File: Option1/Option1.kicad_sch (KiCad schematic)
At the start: 0 parts

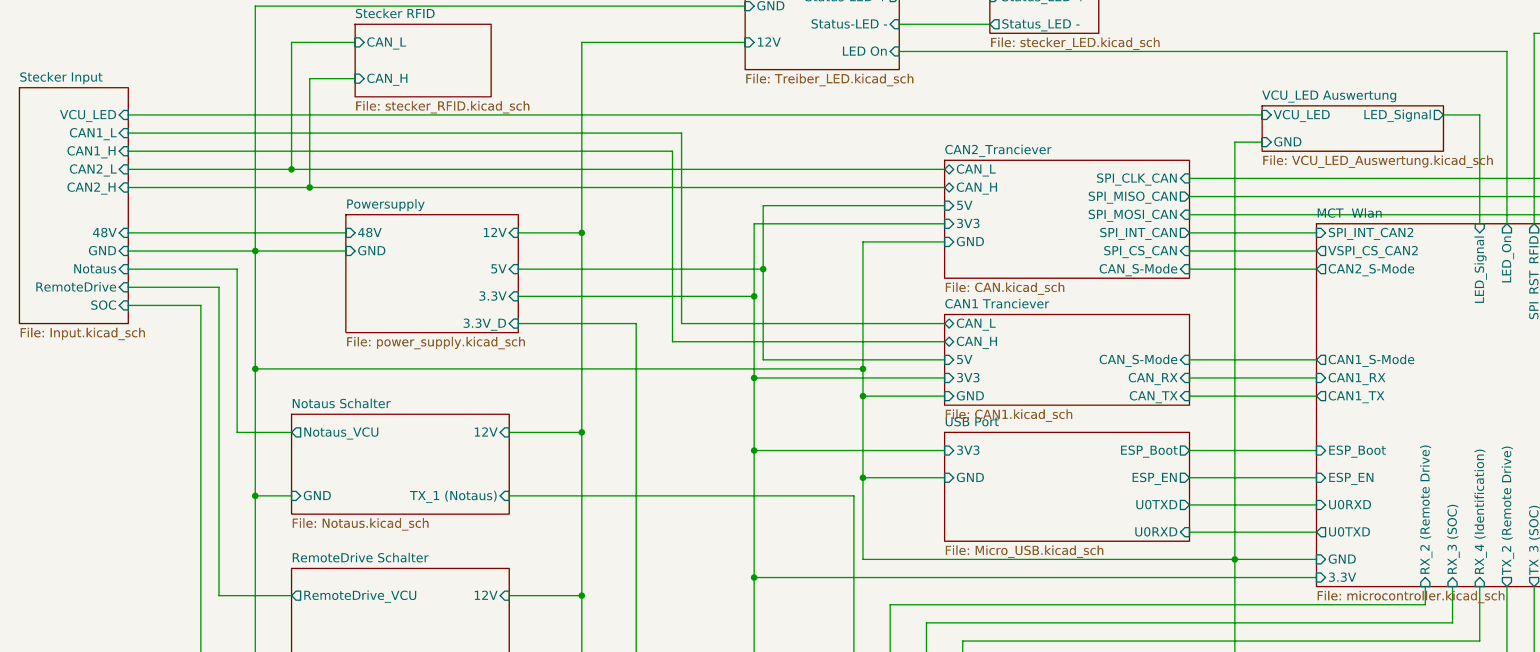
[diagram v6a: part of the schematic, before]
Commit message: USB Schaltung angepasst, Transistoren korrigiert, Stecker ausgetauscht, Dioden hinzugefügt
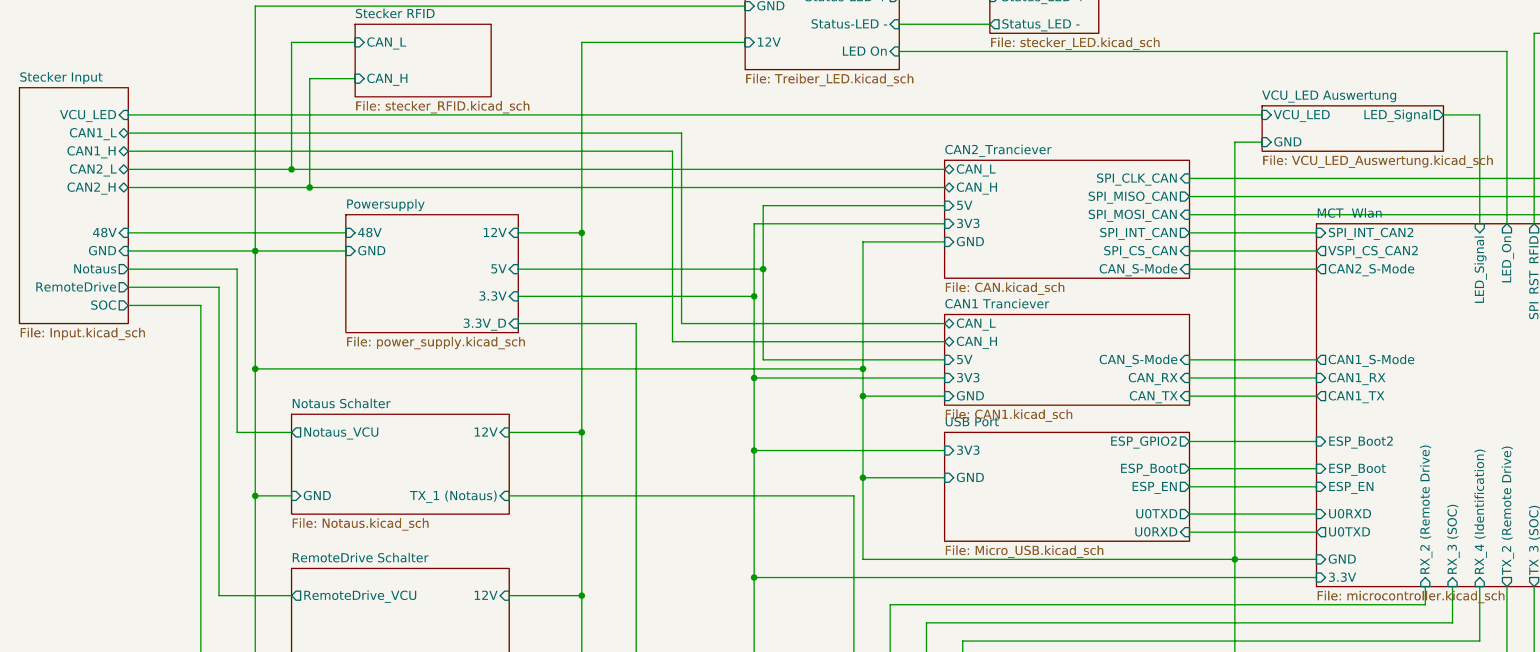
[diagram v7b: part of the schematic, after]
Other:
- sheet MCT  Wlan ports: added ESP_Boot2; removed none
- sheet USB Port ports: added ESP_GPIO2; removed none
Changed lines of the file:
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@@
 	(wire
 		(pts
-			(xy 187.96 83.82) (xy 205.74 83.82)
+			(xy 187.96 86.36) (xy 205.74 86.36)
 		)
 		(stroke
@@
 	(wire
 		(pts
+			(xy 187.96 88.9) (xy 205.74 88.9)
+		)
+		(stroke
+			(width 0)
+			(type default)
+		)
+	)
+	(wire
+		(pts
 			(xy 57.15 72.39) (xy 142.24 72.39)
 		)
@@
 	(wire
 		(pts
-			(xy 187.96 91.44) (xy 205.74 91.44)
-		)
-		(stroke
-			(width 0)
-			(type default)
-		)
-	)
-	(wire
-		(pts
 			(xy 39.37 36.83) (xy 198.12 36.83)
 		)
@@
 	(wire
 		(pts
-			(xy 205.74 87.63) (xy 187.96 87.63)
-		)
-		(stroke
-			(width 0)
-			(type default)
-		)
-	)
-	(wire
-		(pts
 			(xy 261.62 73.66) (xy 264.16 73.66)
 		)
@@
 	(wire
 		(pts
+			(xy 187.96 82.55) (xy 205.74 82.55)
+		)
+		(stroke
+			(width 0)
+			(type default)
+		)
+	)
+	(wire
+		(pts
 			(xy 92.71 113.03) (xy 232.41 113.03)
 		)
@@
 			(type default)
 			(color 0 133 255 1)
+		)
+	)
+	(wire
+		(pts
+			(xy 187.96 92.71) (xy 205.74 92.71)
+		)
+		(stroke
+			(width 0)
+			(type default)
 		)
 	)
@@
 		)
 		(pin "U0TXD" output
-			(at 187.96 91.44 0)
+			(at 187.96 92.71 0)
 			(effects
 				(font
@@
 		)
 		(pin "ESP_EN" output
-			(at 187.96 87.63 0)
+			(at 187.96 88.9 0)
 			(effects
 				(font
@@
 		)
 		(pin "ESP_Boot" output
-			(at 187.96 83.82 0)
+			(at 187.96 86.36 0)
 			(effects
 				(font
@@
 				)
 				(justify left)
+			)
+		)
+		(pin "ESP_GPIO2" output
+			(at 187.96 82.55 0)
+			(effects
+				(font
+					(size 1.27 1.27)
+				)
+				(justify right)
 			)
 		)
@@
 		)
 		(pin "ESP_EN" input
-			(at 205.74 87.63 180)
+			(at 205.74 88.9 180)
 			(effects
 				(font
@@
 		)
 		(pin "ESP_Boot" input
-			(at 205.74 83.82 180)
+			(at 205.74 86.36 180)
 			(effects
 				(font
@@
 		)
 		(pin "U0RXD" input
-			(at 205.74 91.44 180)
+			(at 205.74 92.71 180)
 			(effects
 				(font
@@
 		(pin "SPI_INT_CAN2" input
 			(at 205.74 53.34 180)
+			(effects
+				(font
+					(size 1.27 1.27)
+				)
+				(justify left)
+			)
+		)
+		(pin "ESP_Boot2" input
+			(at 205.74 82.55 180)
 			(effects
 				(font
@@
 			)
 		)
-		(pin "CAN2_L" input
-			(at 39.37 44.45 0)
-			(effects
-				(font
-					(size 1.27 1.27)
-				)
-				(justify right)
-			)
-		)
 		(pin "48V" input
 			(at 39.37 53.34 0)
@@
 			)
 		)
-		(pin "CAN2_H" input
-			(at 39.37 46.99 0)
-			(effects
-				(font
-					(size 1.27 1.27)
-				)
-				(justify right)
-			)
-		)
-		(pin "Notaus" input
-			(at 39.37 58.42 0)
-			(effects
-				(font
-					(size 1.27 1.27)
-				)
-				(justify right)
-			)
-		)
 		(pin "GND" input
 			(at 39.37 55.88 0)
@@
 			)
 		)
-		(pin "SOC" input
-			(at 39.37 63.5 0)
-			(effects
-				(font
-					(size 1.27 1.27)
-				)
-				(justify right)
-			)
-		)
-		(pin "RemoteDrive" input
-			(at 39.37 60.96 0)
-			(effects
-				(font
-					(size 1.27 1.27)
-				)
-				(justify right)
-			)
-		)
 		(pin "VCU_LED" input
 			(at 39.37 36.83 0)
@@
 			)
 		)
-		(pin "CAN1_H" input
+		(pin "CAN2_L" bidirectional
+			(at 39.37 44.45 0)
+			(effects
+				(font
+					(size 1.27 1.27)
+				)
+				(justify right)
+			)
+		)
+		(pin "RemoteDrive" output
+			(at 39.37 60.96 0)
+			(effects
+				(font
+					(size 1.27 1.27)
+				)
+				(justify right)
+			)
+		)
+		(pin "SOC" output
+			(at 39.37 63.5 0)
+			(effects
+				(font
+					(size 1.27 1.27)
+				)
+				(justify right)
+			)
+		)
+		(pin "CAN2_H" bidirectional
+			(at 39.37 46.99 0)
+			(effects
+				(font
+					(size 1.27 1.27)
+				)
+				(justify right)
+			)
+		)
+		(pin "CAN1_H" bidirectional
 			(at 39.37 41.91 0)
 			(effects
@@
 			)
 		)
-		(pin "CAN1_L" input
+		(pin "CAN1_L" bidirectional
 			(at 39.37 39.37 0)
 			(effects
 				(font
+					(size 1.27 1.27)
+				)
+				(justify right)
+			)
+		)
+		(pin "Notaus" output
+			(at 39.37 58.42 0)
+			(effects
+				(font

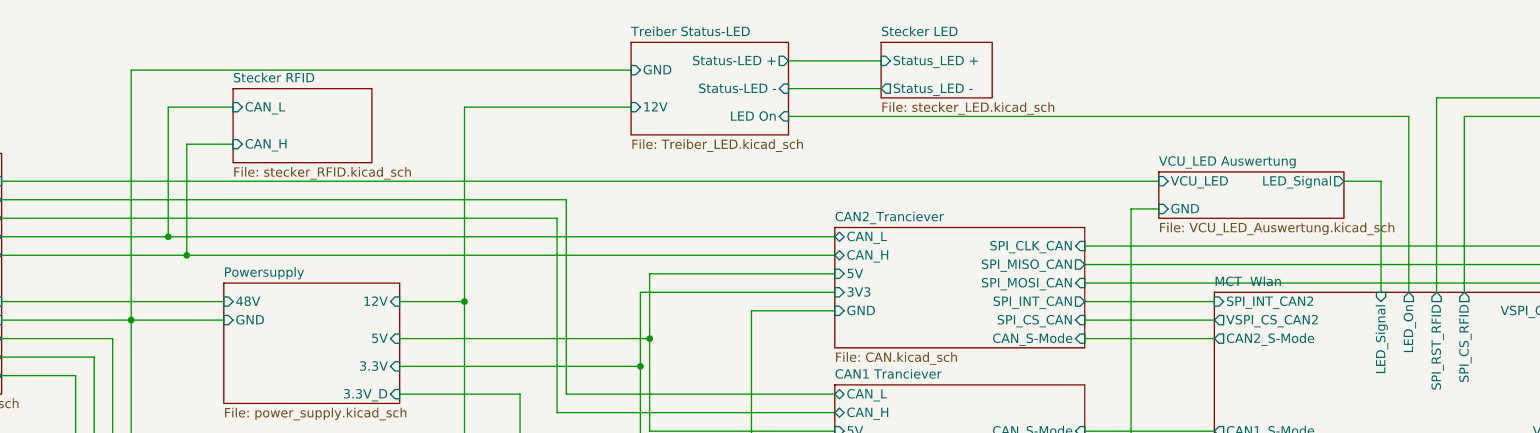
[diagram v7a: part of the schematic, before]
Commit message: Layout komplett bis auf RFID Leiste und 3V3 Erzeugung Display
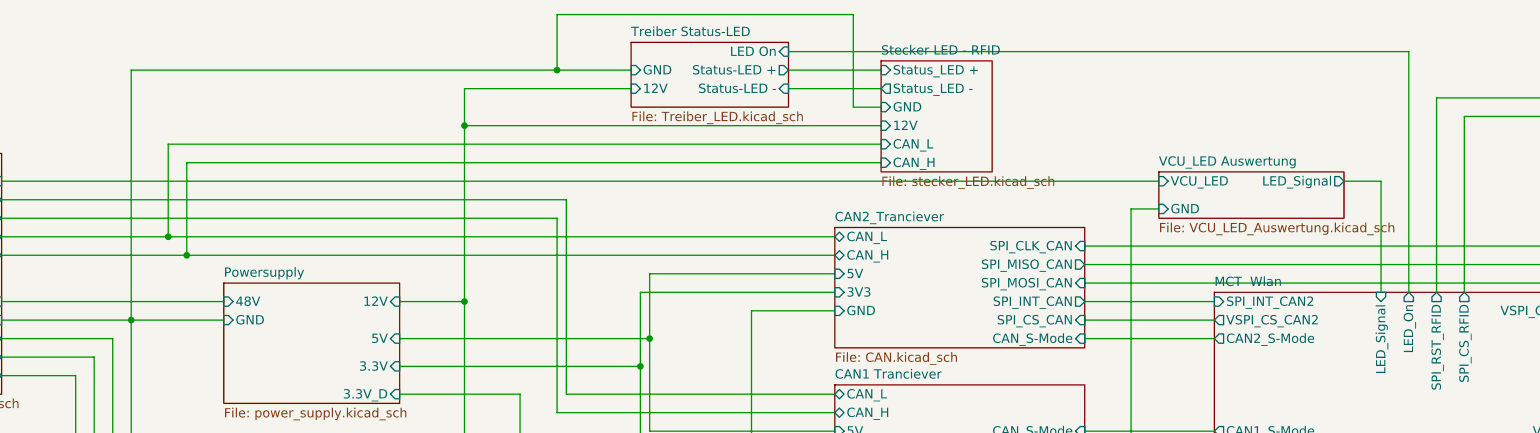
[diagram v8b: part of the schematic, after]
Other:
- sheet Stecker LED renamed Stecker LED - RFID
- removed sheet Stecker RFID
- sheet Stecker LED - RFID ports: added 12V, CAN_H, CAN_L, GND; removed none
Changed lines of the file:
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@@
 	)
 	(junction
+		(at 115.57 21.59)
+		(diameter 0)
+		(color 0 0 0 0)
+	)
+	(junction
 		(at 261.62 59.69)
 		(diameter 0)
@@
 	)
 	(junction
+		(at 102.87 29.21)
+		(diameter 0)
+		(color 0 0 0 0)
+	)
+	(junction
 		(at 128.27 58.42)
 		(diameter 0)
@@
 	(wire
 		(pts
-			(xy 71.12 26.67) (xy 62.23 26.67)
+			(xy 62.23 31.75) (xy 160.02 31.75)
 		)
 		(stroke
@@
 	(wire
 		(pts
+			(xy 102.87 29.21) (xy 160.02 29.21)
+		)
+		(stroke
+			(width 0.5)
+			(type default)
+			(color 255 0 4 1)
+		)
+	)
+	(wire
+		(pts
 			(xy 92.71 129.54) (xy 102.87 129.54)
 		)
@@
 	(wire
 		(pts
-			(xy 62.23 26.67) (xy 62.23 44.45)
+			(xy 62.23 31.75) (xy 62.23 44.45)
 		)
 		(stroke
@@
 	(wire
 		(pts
-			(xy 125.73 21.59) (xy 57.15 21.59)
+			(xy 125.73 21.59) (xy 115.57 21.59)
 		)
 		(stroke
@@
 	(wire
 		(pts
-			(xy 125.73 26.67) (xy 102.87 26.67)
+			(xy 125.73 24.13) (xy 102.87 24.13)
 		)
 		(stroke
@@
 	(wire
 		(pts
-			(xy 102.87 26.67) (xy 102.87 53.34)
+			(xy 102.87 24.13) (xy 102.87 29.21)
 		)
 		(stroke
@@
 	(wire
 		(pts
-			(xy 64.77 31.75) (xy 64.77 46.99)
+			(xy 64.77 34.29) (xy 64.77 46.99)
 		)
 		(stroke
@@
 	(wire
 		(pts
-			(xy 147.32 20.32) (xy 160.02 20.32)
+			(xy 147.32 21.59) (xy 160.02 21.59)
 		)
 		(stroke
@@
 	(wire
 		(pts
-			(xy 147.32 27.94) (xy 232.41 27.94)
+			(xy 147.32 19.05) (xy 232.41 19.05)
 		)
 		(stroke
@@
 	(wire
 		(pts
-			(xy 232.41 27.94) (xy 232.41 52.07)
+			(xy 232.41 19.05) (xy 232.41 52.07)
 		)
 		(stroke
@@
 	(wire
 		(pts
+			(xy 115.57 13.97) (xy 156.21 13.97)
+		)
+		(stroke
+			(width 0.5)
+			(type default)
+			(color 0 0 0 1)
+		)
+	)
+	(wire
+		(pts
 			(xy 153.67 71.12) (xy 128.27 71.12)
 		)
@@
 	(wire
 		(pts
-			(xy 71.12 31.75) (xy 64.77 31.75)
+			(xy 64.77 34.29) (xy 160.02 34.29)
 		)
 		(stroke
@@
 	(wire
 		(pts
+			(xy 156.21 13.97) (xy 156.21 26.67)
+		)
+		(stroke
+			(width 0.5)
+			(type default)
+			(color 0 0 0 1)
+		)
+	)
+	(wire
+		(pts
 			(xy 127 62.23) (xy 127 73.66)
 		)
@@
 	(wire
 		(pts
+			(xy 115.57 21.59) (xy 115.57 13.97)
+		)
+		(stroke
+			(width 0.5)
+			(type default)
+			(color 0 0 0 1)
+		)
+	)
+	(wire
+		(pts
 			(xy 102.87 129.54) (xy 102.87 104.14)
 		)
@@
 	(wire
 		(pts
+			(xy 115.57 21.59) (xy 57.15 21.59)
+		)
+		(stroke
+			(width 0.5)
+			(type default)
+			(color 0 0 0 1)
+		)
+	)
+	(wire
+		(pts
 			(xy 260.35 45.72) (xy 260.35 57.15)
 		)
@@
 	(wire
 		(pts
+			(xy 102.87 29.21) (xy 102.87 53.34)
+		)
+		(stroke
+			(width 0.5)
+			(type default)
+			(color 255 0 4 1)
+		)
+	)
+	(wire
+		(pts
 			(xy 259.08 54.61) (xy 264.16 54.61)
 		)
@@
 	(wire
 		(pts
+			(xy 156.21 26.67) (xy 160.02 26.67)
+		)
+		(stroke
+			(width 0.5)
+			(type default)
+			(color 0 0 0 1)
+		)
+	)
+	(wire
+		(pts
 			(xy 127 83.82) (xy 153.67 83.82)
 		)
@@
 	)
 	(sheet
-		(at 160.02 17.78)
-		(size 15.24 7.62)
+		(at 160.02 20.32)
+		(size 15.24 15.24)
 		(exclude_from_sim no)
 		(in_bom yes)
@@
 			(color 102 255 255 1.0000)
 		)
-		(property "Sheetname" "Stecker LED"
-			(at 160.02 17.0684 0)
+		(property "Sheetname" "Stecker LED - RFID"
+			(at 160.02 19.6084 0)
 			(effects
 				(font
@@
 		)
 		(property "Sheetfile" "stecker_LED.kicad_sch"
-			(at 160.02 25.9846 0)
+			(at 160.02 36.1446 0)
 			(effects
 				(font
@@
 		)
 		(pin "Status_LED +" input
-			(at 160.02 20.32 180)
+			(at 160.02 21.59 180)
+			(effects
+				(font
+					(size 1.27 1.27)
+				)
+				(justify left)
+			)
+		)
+		(pin "12V" input
+			(at 160.02 29.21 180)
+			(effects
+				(font
+					(size 1.27 1.27)
+				)
+				(justify left)
+			)
+		)
+		(pin "GND" input
+			(at 160.02 26.67 180)
+			(effects
+				(font
+					(size 1.27 1.27)
+				)
+				(justify left)
+			)
+		)
+		(pin "CAN_L" input
+			(at 160.02 31.75 180)
+			(effects
+				(font
+					(size 1.27 1.27)
+				)
+				(justify left)
+			)
+		)
+		(pin "CAN_H" input
+			(at 160.02 34.29 180)
 			(effects
 				(font
@@
 	(sheet
 		(at 125.73 17.78)
-		(size 21.59 12.7)
+		(size 21.59 8.89)
 		(exclude_from_sim no)
 		(in_bom yes)
@@
 		)
 		(property "Sheetfile" "Treiber_LED.kicad_sch"
-			(at 125.73 31.0646 0)
+			(at 125.73 27.2546 0)
 			(effects
 				(font
@@
 		)
 		(pin "12V" input
-			(at 125.73 26.67 180)
+			(at 125.73 24.13 180)
 			(effects
 				(font
@@
 		)
 		(pin "LED On" input
-			(at 147.32 27.94 0)
+			(at 147.32 19.05 0)
 			(effects
 				(font
@@
 		)
 		(pin "Status-LED +" output
-			(at 147.32 20.32 0)
+			(at 147.32 21.59 0)
 			(effects
 				(font
@@
 				)
 			)
-		)
-	)
-	(sheet
-		(at 71.12 24.13)
-		(size 19.05 10.16)
-		(exclude_from_sim no)
-		(in_bom yes)
-		(on_board yes)
-		(dnp no)
-		(fields_autoplaced yes)
-		(stroke
-			(width 0.1524)
-			(type solid)
-		)
-		(fill
-			(color 102 255 255 1.0000)
-		)
-		(property "Sheetname" "Stecker RFID"
-			(at 71.12 23.4184 0)
-			(effects
-				(font
-					(size 1.27 1.27)
-				)
-				(justify left bottom)
-			)
-		)
-		(property "Sheetfile" "stecker_RFID.kicad_sch"
-			(at 71.12 34.8746 0)
-			(effects
-				(font
-					(size 1.27 1.27)
-				)
-				(justify left top)
-			)
-		)
-		(pin "CAN_L" input
-			(at 71.12 26.67 180)
-			(effects
-				(font
-					(size 1.27 1.27)
-				)
-				(justify left)
-			)
-		)
-		(pin "CAN_H" input
-			(at 71.12 31.75 180)
-			(effects
-				(font
-					(size 1.27 1.27)
-				)
-				(justify left)
-			)
-		)
-		(instances
-			(project "Option1"
-				(path "/b9e5f262-9648-4b79-bdd1-af888b822329"
-					(page "13")
-				)
-			)
